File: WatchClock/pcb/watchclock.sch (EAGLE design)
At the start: 31 parts, among them IC1 MEGA32-A, Q2 BSP170P

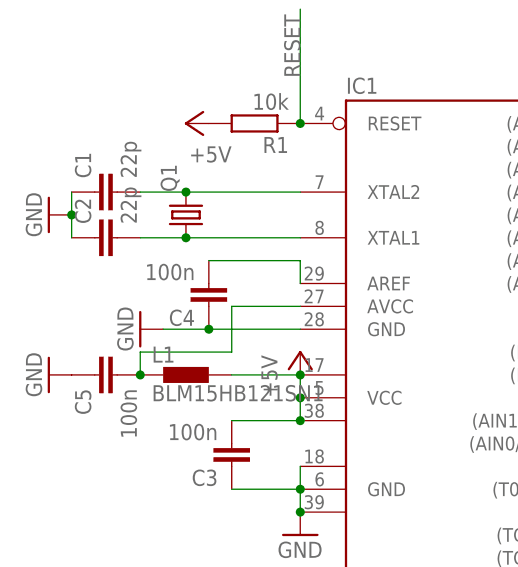
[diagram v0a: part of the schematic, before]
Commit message: WatchClock PCB: Routing complete
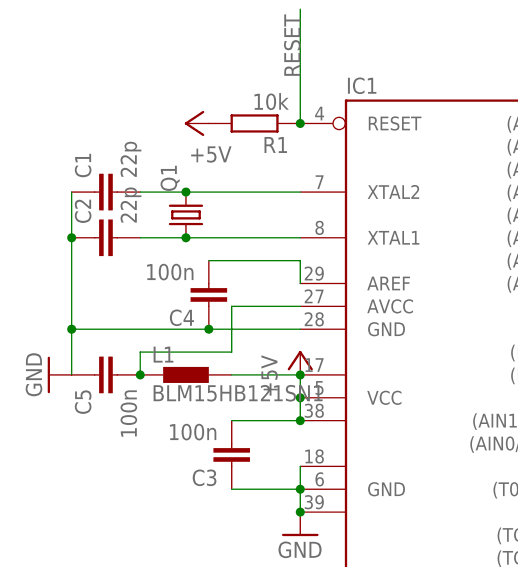
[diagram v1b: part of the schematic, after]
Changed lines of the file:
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@@
 <part name="GND1" library="supply1" deviceset="GND" device=""/>
 <part name="P+1" library="supply1" deviceset="+5V" device=""/>
-<part name="GND2" library="supply1" deviceset="GND" device=""/>
 <part name="P+2" library="supply1" deviceset="+5V" device=""/>
-<part name="GND3" library="supply1" deviceset="GND" device=""/>
 <part name="C4" library="resistor" deviceset="C-EU" device="C0805" value="100n"/>
 <part name="GND4" library="supply1" deviceset="GND" device=""/>
@@
 <instance part="GND1" gate="1" x="45.72" y="40.64"/>
 <instance part="P+1" gate="1" x="45.72" y="60.96"/>
-<instance part="GND2" gate="1" x="17.78" y="76.2" rot="R270"/>
 <instance part="P+2" gate="1" x="33.02" y="86.36" rot="R90"/>
-<instance part="GND3" gate="1" x="27.94" y="63.5" rot="R270"/>
 <instance part="C4" gate="G$1" x="35.56" y="66.04" rot="R180"/>
 <instance part="GND4" gate="1" x="129.54" y="53.34"/>
@@
 <pinref part="C1" gate="G$1" pin="1"/>
 <pinref part="C2" gate="G$1" pin="1"/>
-<wire x1="20.32" y1="78.74" x2="20.32" y2="76.2" width="0.1524" layer="91"/>
-<pinref part="GND2" gate="1" pin="GND"/>
-<junction x="20.32" y="76.2"/>
-<wire x1="20.32" y1="76.2" x2="20.32" y2="73.66" width="0.1524" layer="91"/>
-</segment>
-<segment>
+<wire x1="20.32" y1="78.74" x2="20.32" y2="73.66" width="0.1524" layer="91"/>
 <pinref part="IC1" gate="G$1" pin="GND@1"/>
-<pinref part="GND3" gate="1" pin="GND"/>
-<wire x1="30.48" y1="63.5" x2="35.56" y2="63.5" width="0.1524" layer="91"/>
+<wire x1="20.32" y1="63.5" x2="35.56" y2="63.5" width="0.1524" layer="91"/>
 <pinref part="C4" gate="G$1" pin="1"/>
 <wire x1="35.56" y1="63.5" x2="45.72" y2="63.5" width="0.1524" layer="91"/>
 <junction x="35.56" y="63.5"/>
+<wire x1="20.32" y1="73.66" x2="20.32" y2="63.5" width="0.1524" layer="91"/>
+<pinref part="C5" gate="G$1" pin="1"/>
+<pinref part="GND5" gate="1" pin="GND"/>
+<wire x1="20.32" y1="63.5" x2="20.32" y2="58.42" width="0.1524" layer="91"/>
+<junction x="20.32" y="73.66"/>
+<junction x="20.32" y="63.5"/>
 </segment>
 <segment>
@@
 </segment>
 <segment>
-<pinref part="C5" gate="G$1" pin="1"/>
-<pinref part="GND5" gate="1" pin="GND"/>
-</segment>
-<segment>

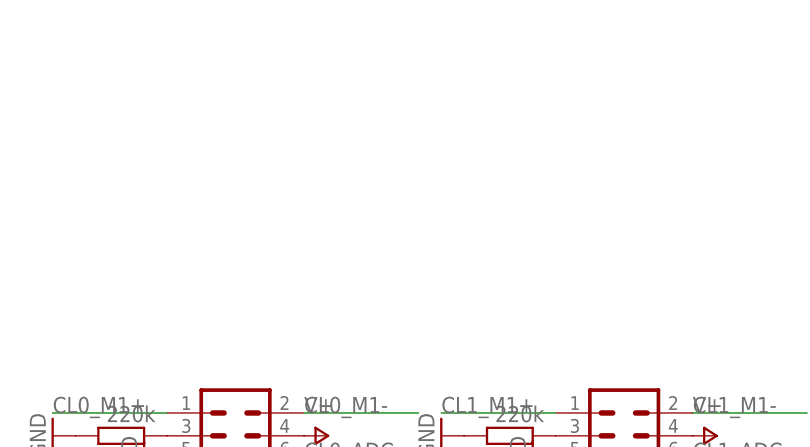
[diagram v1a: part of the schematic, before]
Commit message: Update WatchClock PCB
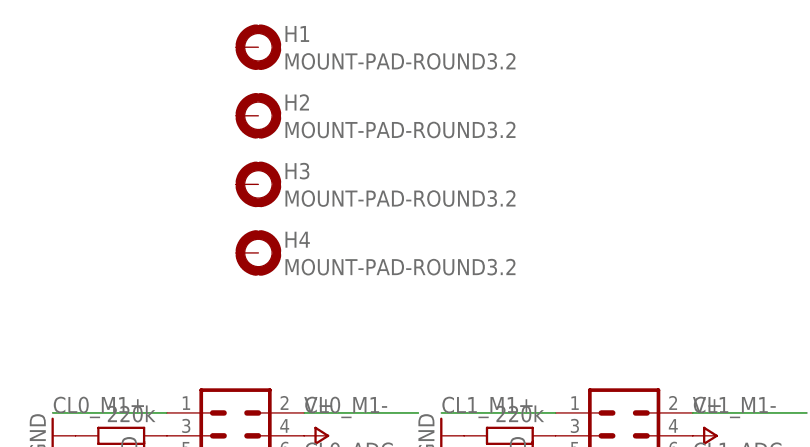
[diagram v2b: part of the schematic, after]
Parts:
- added H1, H2, H3, H4: MOUNT-PAD-ROUND3.2, holes:MOUNT-PAD-ROUND3.2
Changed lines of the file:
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@@
 <part name="R14" library="resistor" deviceset="R-EU_" device="M0805" value="10k"/>
 <part name="P+18" library="supply1" deviceset="V+" device=""/>
+<part name="H1" library="holes" deviceset="MOUNT-PAD-ROUND" device="3.2"/>
+<part name="H2" library="holes" deviceset="MOUNT-PAD-ROUND" device="3.2"/>
+<part name="H3" library="holes" deviceset="MOUNT-PAD-ROUND" device="3.2"/>
+<part name="H4" library="holes" deviceset="MOUNT-PAD-ROUND" device="3.2"/>
 </parts>
 <sheets>
@@
 <instance part="R14" gate="G$1" x="114.3" y="2.54" rot="R180"/>
 <instance part="P+18" gate="1" x="124.46" y="-7.62" rot="R180"/>
+<instance part="H1" gate="G$1" x="170.18" y="116.84"/>
+<instance part="H2" gate="G$1" x="170.18" y="109.22"/>
+<instance part="H3" gate="G$1" x="170.18" y="101.6"/>
+<instance part="H4" gate="G$1" x="170.18" y="93.98"/>
 </instances>
 <busses>
